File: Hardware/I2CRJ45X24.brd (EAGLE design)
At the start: 216 x 50 mm, 82 parts, among them IC1 MCP23017SO, IC2 MCP23017SO, IC3 MCP23017SO, IC4 MCP23017SO, IC5 MCP23017SO, IC6 MCP23017SO, J1 I2C-BREAKOUT, J2 I2C-BREAKOUT, J3 M01-PLAIN, J4 RJ45-X8, J5 RJ45-X8, J6 RJ45-X8

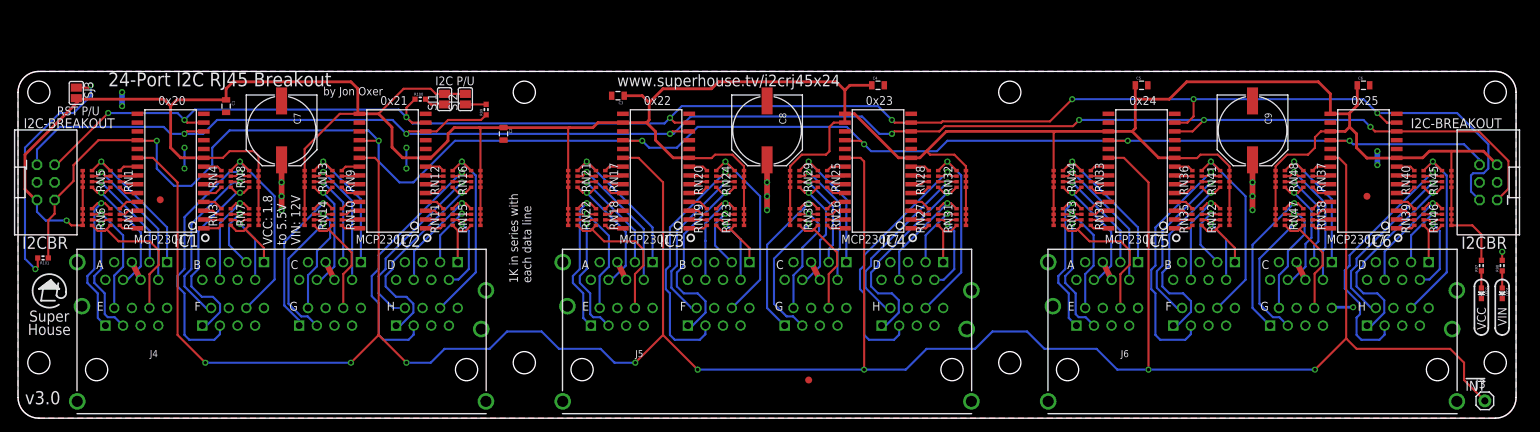
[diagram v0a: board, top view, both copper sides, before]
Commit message: Major rework: rerouted entire board.
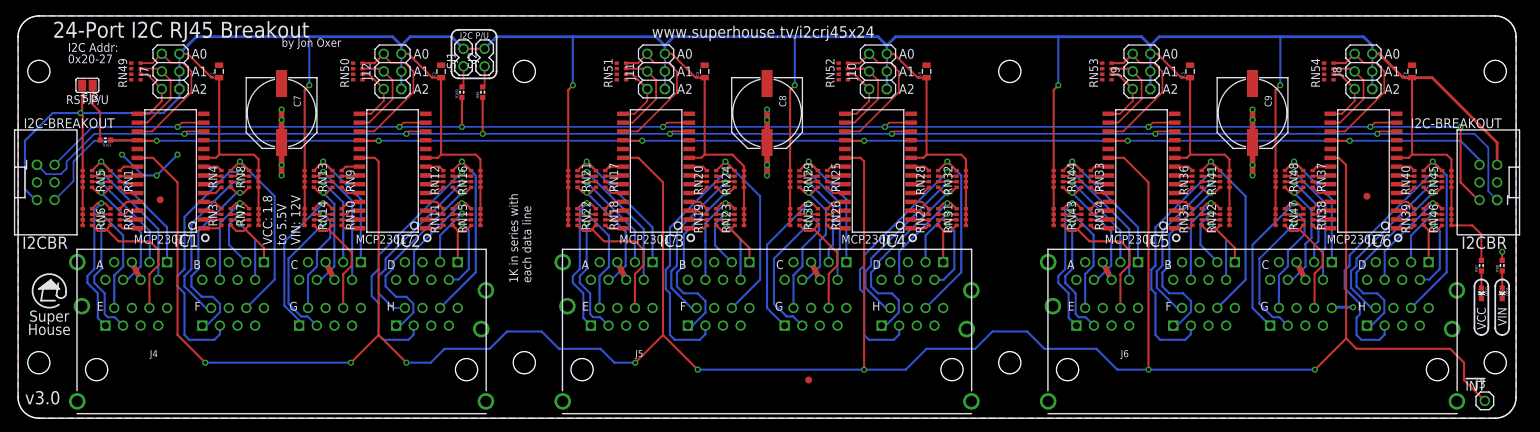
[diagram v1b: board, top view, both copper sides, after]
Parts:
- added J10: I2C Addr 4, SuperHouse-Connectors:2X03-P
- added J11: I2C Addr 3, SuperHouse-Connectors:2X03-P
- added J12: I2C Addr 2, SuperHouse-Connectors:2X03-P
- added J7: I2C Addr 1, SuperHouse-Connectors:2X03-P
- added J8: I2C Addr 6, SuperHouse-Connectors:2X03-P
- added J9: I2C Addr 5, SuperHouse-Connectors:2X03-P
- added RN49, RN50, RN51, RN52, RN53, RN54: 10K, SuperHouse-Resistors:CAY16
- J1, J2: device SuperHouse-Connectors:2X03-SHROUDED -> SuperHouse-Connectors:2X3-2.54-SHROUDED
- SJ1, SJ2: device SuperHouse-Jumpers:SJ -> SuperHouse-Connectors:1X02-P
- moved R101 19.2 mm to (12.6, 40.1)
- moved C3 13.0 mm to (99.0, 50.0), turned to 90 degrees
- moved C2 12.7 mm to (61.0, 50.0), turned to 90 degrees
- moved C4 7.28 mm to (131.0, 50.0), turned to 90 degrees
- moved C5 7.28 mm to (169.0, 50.0), turned to 90 degrees
- moved C6 7.28 mm to (201.0, 50.0), turned to 90 degrees
- moved SJ2 6.61 mm to (67.3, 52.0)
- moved SJ1 6.59 mm to (64.2, 52.0)
- moved R100 6.08 mm to (64.0, 47.0), turned to 90 degrees
- moved C1 5.10 mm to (29.0, 50.0), turned to 90 degrees
- moved R99 2.55 mm to (67.0, 47.0)
- moved C7 2.50 mm to (38.0, 44.0)
- moved C8 2.50 mm to (108.0, 44.0)
- moved C9 2.50 mm to (178.0, 44.0)
- moved SJ3 1.94 mm to (10.0, 48.0), turned to 180 degrees
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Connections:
- new net N$10: IC2.16, J12.4, RN50.7
- new net N$11: IC2.17, J12.6, RN50.8
- new net N$12: IC3.17, J11.6, RN51.8
- new net N$13: IC3.15, J11.2, RN51.6
- new net N$14: IC3.16, J11.4, RN51.7
- new net N$15: IC4.17, J10.6, RN52.8
- new net N$16: IC4.15, J10.2, RN52.6
- new net N$17: IC4.16, J10.4, RN52.7
- new net N$18: IC5.17, J9.6, RN53.8
- new net N$19: IC5.15, J9.2, RN53.6
- new net N$20: IC5.16, J9.4, RN53.7
- new net N$21: IC6.17, J8.6, RN54.8
- new net N$22: IC6.15, J8.2, RN54.6
- new net N$23: IC6.16, J8.4, RN54.7
- new net N$4: IC1.17, J7.6, RN49.8
- new net N$5: IC1.16, J7.4, RN49.7
- new net N$6: IC1.15, J7.2, RN49.6
- new net N$9: IC2.15, J12.2, RN50.6
- net GND: now also RN49.1, RN49.2, RN49.3, RN49.4, RN50.1, RN50.2, RN50.3, RN50.4, RN51.1, RN51.2, RN51.3, RN51.4, RN52.1, RN52.2, RN52.3, RN52.4, RN53.1, RN53.2, RN53.3, RN53.4, RN54.1, RN54.2, RN54.3, RN54.4; no longer IC1.15, IC1.16, IC1.17, IC2.16, IC2.17, IC3.15, IC3.17, IC4.17, IC5.15, IC5.16, IC6.16
- net VCC: now also J10.1, J10.3, J10.5, J11.1, J11.3, J11.5, J12.1, J12.3, J12.5, J7.1, J7.3, J7.5, J8.1, J8.3, J8.5, J9.1, J9.3, J9.5; no longer IC2.15, IC3.16, IC4.15, IC4.16, IC5.17, IC6.15, IC6.17
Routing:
- net VCC: track 533.8 -> 653.1 mm, vias 1 -> 6
- net N$3: track 36.2 -> 8.35 mm, vias 2 -> 0
- net !RESET: track 256.2 -> 233.2 mm
- net N$12: track 0.00 -> 22.1 mm
- net N$11: track 0.00 -> 22.1 mm
- net N$18: track 0.00 -> 22.1 mm
- net N$4: track 0.00 -> 22.1 mm
- net N$21: track 0.00 -> 22.1 mm
- net N$15: track 0.00 -> 22.0 mm
- net N$17: track 0.00 -> 13.9 mm
- net N$14: track 0.00 -> 13.9 mm
- net N$10: track 0.00 -> 13.9 mm
- net N$5: track 0.00 -> 13.9 mm
- net N$23: track 0.00 -> 13.9 mm
- net N$20: track 0.00 -> 13.9 mm
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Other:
- board size 216 x 50 mm -> 216 x 58 mm
- board text added: "A0"
- board text added: "A1"
- board text added: "A2"
- board text added: "I2C Addr: 0x20-27"
- board text removed: "0x20"
- board text removed: "0x21"
- board text removed: "0x22"
- board text removed: "0x23"
- board text removed: "0x24"
- board text removed: "0x25"
